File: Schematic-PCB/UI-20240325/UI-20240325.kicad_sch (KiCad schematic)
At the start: 0 parts

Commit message: UI基板の回路図を更新
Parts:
- added BZ1: Buzzer, symbol Device:Buzzer
- added J1: Conn_01x10_Pin, symbol Connector:Conn_01x10_Pin
- added R1, R3, R5, R6, R9: 1K, symbol Device:R_Small
- added R10, R2, R4, R7, R8: 10K, symbol Device:R_Small
- added SW1, SW2: SW_SPDT, symbol Switch:SW_SPDT
- added SW3, SW4, SW5: SW_Push, symbol Switch:SW_Push
- added U1: ~, symbol @2024-UI:Display
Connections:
- new net: R5.2, R7.2, SW3.1
- new net: R10.2, R9.2, SW5.1
- new net: R1.2, R2.2, SW1.2 (B)
- new net: R3.2, R4.2, SW2.2 (B)
- new net: R6.2, R8.2, SW4.1
- new net +3.3V: J1.1 (Pin_1), SW1.1 (A), SW2.1 (A), SW3.2, SW4.2, SW5.2, U1. (VCC)
- new net BUZZER: BZ1.1 (+), J1.10 (Pin_10)
- new net GND: BZ1.2 (-), J1.2 (Pin_2), R10.1, R2.1, R4.1, R7.1, R8.1, U1. (VCC)
- new net SCL: J1.9 (Pin_9), U1. (VCC)
- new net SDA: J1.8 (Pin_8), U1. (VCC)
- new net SW-TAC-1: J1.5 (Pin_5), R5.1
- new net SW-TAC-2: J1.6 (Pin_6), R6.1
- new net SW-TAC-3: J1.7 (Pin_7), R9.1
- new net SW-TOG-1: J1.4 (Pin_4), R1.1
- new net SW-TOG-2: J1.3 (Pin_3), R3.1
- no-connect marks 0 -> 2
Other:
- note added: "BUZZER"
- note added: "DISPLAY"
- note added: "TACTILE"
- note added: "TO MAIN"
- note added: "TOGGLE"

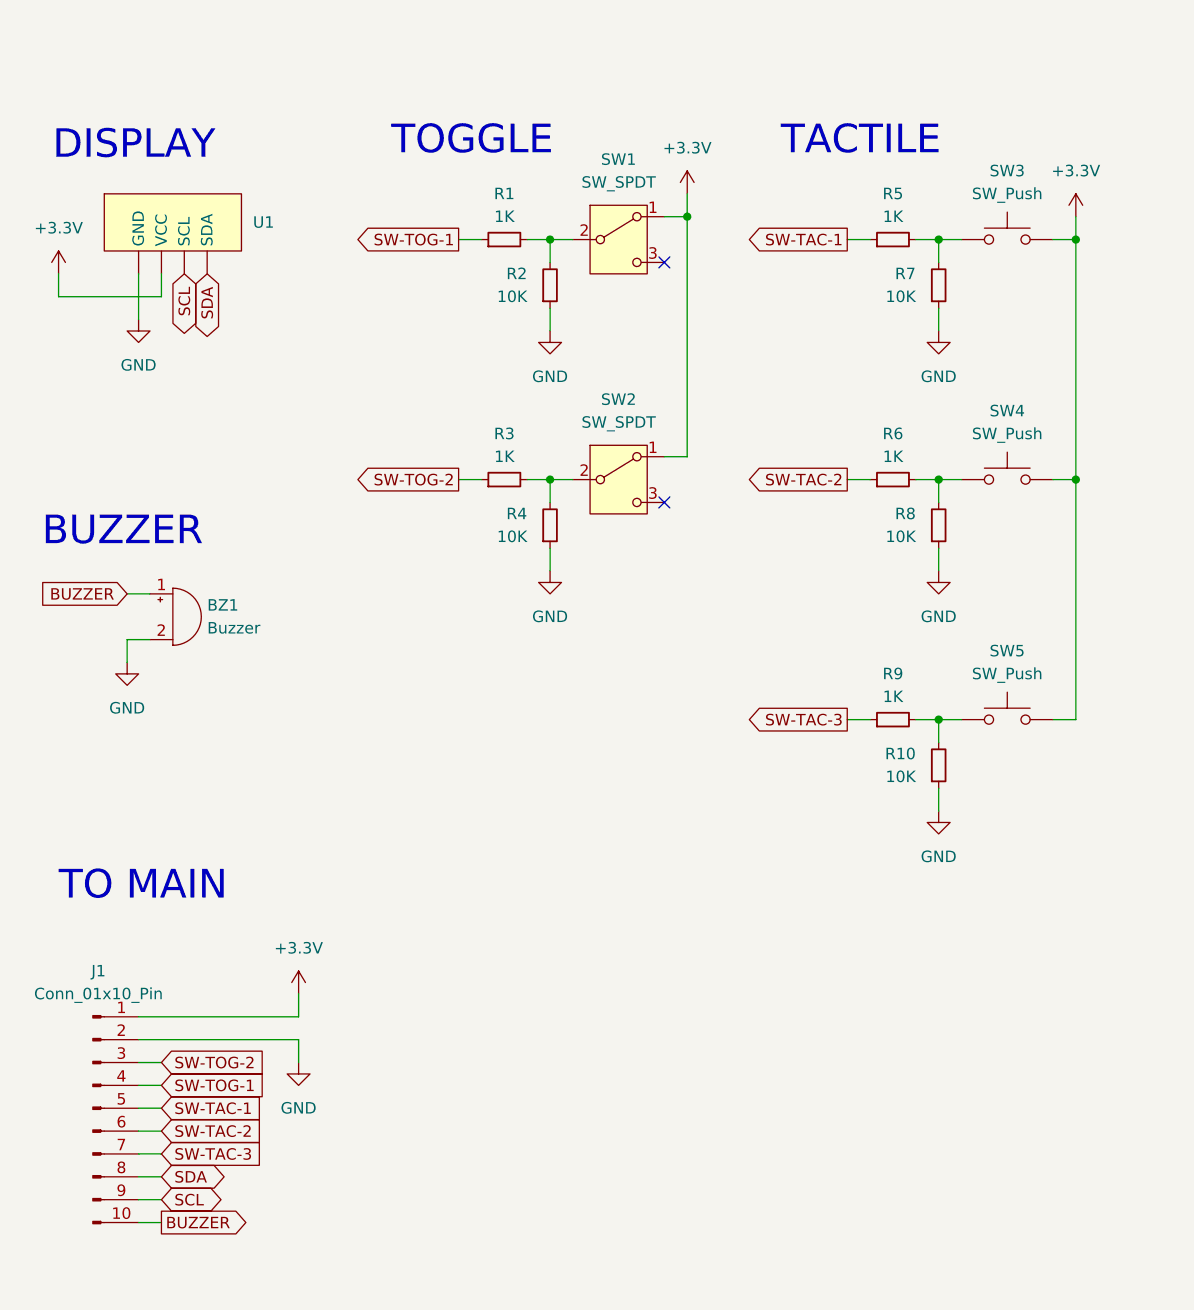
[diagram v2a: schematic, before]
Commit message: UI基板のPCBデザインを作成
決定ボタンのみフットプリントが決定しておらず未完成
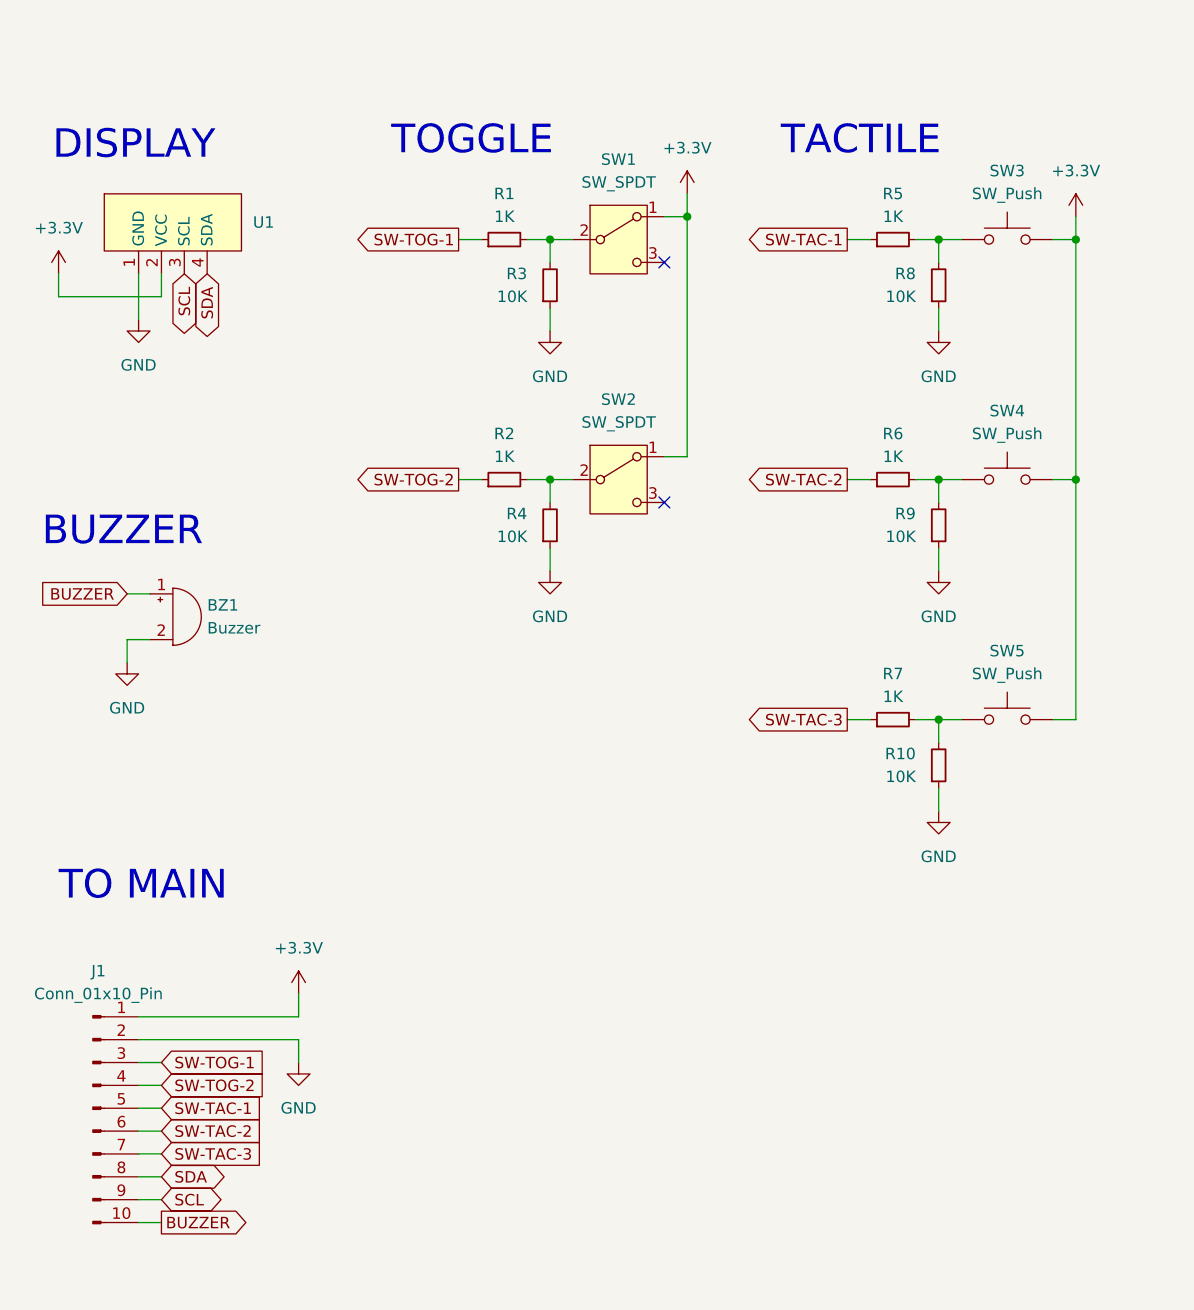
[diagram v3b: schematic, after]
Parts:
- BZ1: footprint (none) -> @2024-UI:PKM13EPYH4000-A0
- J1: footprint (none) -> Connector_JST:JST_XH_B10B-XH-A_1x10_P2.50mm_Vertical
- R1, R10, R4, R5, R6: footprint (none) -> Resistor_SMD:R_0603_1608Metric
- R2: renamed from R3; footprint (none) -> Resistor_SMD:R_0603_1608Metric
- R3: renamed from R2; footprint (none) -> Resistor_SMD:R_0603_1608Metric
- R7: renamed from R9; footprint (none) -> Resistor_SMD:R_0603_1608Metric
- R8: renamed from R7; footprint (none) -> Resistor_SMD:R_0603_1608Metric
- R9: renamed from R8; footprint (none) -> Resistor_SMD:R_0603_1608Metric
- SW1, SW2: footprint (none) -> @2024-UI:2MS1-T1-B4-VS2-Q-E-S
- SW3, SW5: footprint (none) -> @2024-UI:TVBP06-B043C
- U1: footprint (none) -> @2024-UI:Display
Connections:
- net +3.3V: now also U1.2 (VCC); no longer U1. (VCC)
- net GND: now also U1.1 (GND); no longer U1. (VCC)
- net SCL: now also U1.3 (SCL); no longer U1. (VCC)
- net SDA: now also U1.4 (SDA); no longer U1. (VCC)
- net SW-TOG-1: now also J1.3 (Pin_3); no longer J1.4 (Pin_4)
- net SW-TOG-2: now also J1.4 (Pin_4); no longer J1.3 (Pin_3)

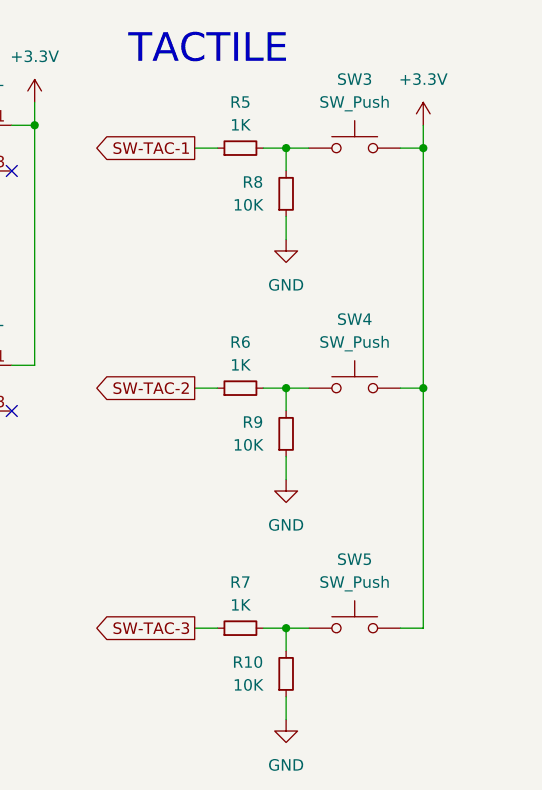
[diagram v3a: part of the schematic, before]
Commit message: Ui基板の回路図・PCBデザインを更新しました
DR & 修正・SW-4に関する変更
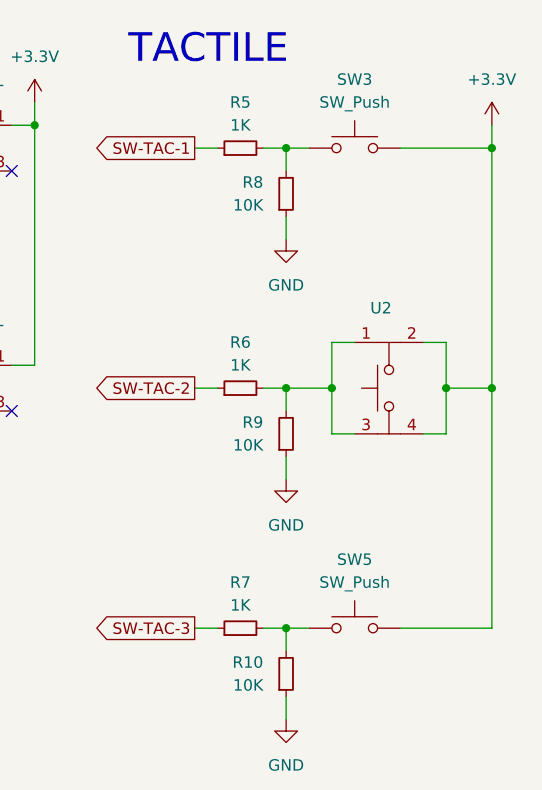
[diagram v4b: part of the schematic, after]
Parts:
- removed SW4: SW_Push, symbol Switch:SW_Push
- added U2: ~, @2024-UI:TVGP01-G73BB, symbol @2024-UI:TVGP01-G73BB
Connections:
- net +3.3V: now also U2.2, U2.4
- net at R6.2, R9.2: now also U2.1, U2.3
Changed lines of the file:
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@@
 	(paper "A4")
 	(junction
-		(at 140.97 50.8)
+		(at 148.59 50.8)
+		(diameter 0)
+		(color 0 0 0 0)
+	)
+	(junction
+		(at 148.59 77.47)
 		(diameter 0)
 		(color 0 0 0 0)
@@
 	)
 	(junction
-		(at 140.97 77.47)
+		(at 143.51 77.47)
 		(diameter 0)
 		(color 0 0 0 0)
@@
 		(color 0 0 0 0)
 	)
+	(junction
+		(at 130.81 77.47)
+		(diameter 0)
+		(color 0 0 0 0)
+	)
 	(no_connect
 		(at 95.25 80.01)
@@
 	(wire
 		(pts
+			(xy 133.35 82.55) (xy 130.81 82.55)
+		)
+		(stroke
+			(width 0)
+			(type default)
+		)
+	)
+	(wire
+		(pts
 			(xy 82.55 53.34) (xy 82.55 50.8)
 		)
@@
 	(wire
 		(pts
-			(xy 140.97 50.8) (xy 140.97 77.47)
+			(xy 148.59 50.8) (xy 148.59 77.47)
 		)
 		(stroke
@@
 	(wire
 		(pts
-			(xy 138.43 50.8) (xy 140.97 50.8)
-		)
-		(stroke
-			(width 0)
-			(type default)
-		)
-	)
-	(wire
-		(pts
-			(xy 138.43 77.47) (xy 140.97 77.47)
-		)
-		(stroke
-			(width 0)
-			(type default)
-		)
-	)
-	(wire
-		(pts
 			(xy 36.83 154.94) (xy 39.37 154.94)
 		)
@@
 	(wire
 		(pts
-			(xy 138.43 104.14) (xy 140.97 104.14)
-		)
-		(stroke
-			(width 0)
-			(type default)
-		)
-	)
-	(wire
-		(pts
 			(xy 72.39 50.8) (xy 74.93 50.8)
 		)
@@
 	(wire
 		(pts
+			(xy 140.97 72.39) (xy 143.51 72.39)
+		)
+		(stroke
+			(width 0)
+			(type default)
+		)
+	)
+	(wire
+		(pts
 			(xy 36.83 54.61) (xy 36.83 59.69)
 		)
@@
 	(wire
 		(pts
+			(xy 143.51 77.47) (xy 148.59 77.47)
+		)
+		(stroke
+			(width 0)
+			(type default)
+		)
+	)
+	(wire
+		(pts
 			(xy 123.19 104.14) (xy 125.73 104.14)
 		)
@@
 	(wire
 		(pts
+			(xy 138.43 104.14) (xy 148.59 104.14)
+		)
+		(stroke
+			(width 0)
+			(type default)
+		)
+	)
+	(wire
+		(pts
 			(xy 115.57 104.14) (xy 118.11 104.14)
 		)
@@
 	(wire
 		(pts
-			(xy 140.97 77.47) (xy 140.97 104.14)
+			(xy 130.81 82.55) (xy 130.81 77.47)
 		)
 		(stroke
@@
 	(wire
 		(pts
-			(xy 140.97 48.26) (xy 140.97 50.8)
+			(xy 148.59 48.26) (xy 148.59 50.8)
 		)
 		(stroke
@@
 	(wire
 		(pts
+			(xy 148.59 77.47) (xy 148.59 104.14)
+		)
+		(stroke
+			(width 0)
+			(type default)
+		)
+	)
+	(wire
+		(pts
+			(xy 143.51 82.55) (xy 140.97 82.55)
+		)
+		(stroke
+			(width 0)
+			(type default)
+		)
+	)
+	(wire
+		(pts
 			(xy 54.61 139.7) (xy 54.61 142.24)
 		)
@@
 	(wire
 		(pts
+			(xy 130.81 72.39) (xy 130.81 77.47)
+		)
+		(stroke
+			(width 0)
+			(type default)
+		)
+	)
+	(wire
+		(pts
 			(xy 39.37 57.15) (xy 27.94 57.15)
 		)
@@
 	(wire
 		(pts
-			(xy 125.73 77.47) (xy 128.27 77.47)
+			(xy 125.73 77.47) (xy 130.81 77.47)
 		)
 		(stroke
@@
 	(wire
 		(pts
+			(xy 143.51 77.47) (xy 143.51 82.55)
+		)
+		(stroke
+			(width 0)
+			(type default)
+		)
+	)
+	(wire
+		(pts
 			(xy 35.56 90.17) (xy 38.1 90.17)
 		)
@@
 	(wire
 		(pts
+			(xy 130.81 72.39) (xy 133.35 72.39)
+		)
+		(stroke
+			(width 0)
+			(type default)
+		)
+	)
+	(wire
+		(pts
 			(xy 36.83 142.24) (xy 39.37 142.24)
+		)
+		(stroke
+			(width 0)
+			(type default)
+		)
+	)
+	(wire
+		(pts
+			(xy 138.43 50.8) (xy 148.59 50.8)
+		)
+		(stroke
+			(width 0)
+			(type default)
+		)
+	)
+	(wire
+		(pts
+			(xy 143.51 72.39) (xy 143.51 77.47)
 		)
 		(stroke
@@
 	(symbol
 		(lib_id "power:+3.3V")
-		(at 140.97 48.26 0)
+		(at 148.59 48.26 0)
 		(unit 1)
 		(exclude_from_sim no)
@@
 		(fields_autoplaced yes)
 		(property "Reference" "#PWR012"
-			(at 140.97 52.07 0)
+			(at 148.59 52.07 0)
 			(effects
 				(font
@@
 		)
 		(property "Value" "+3.3V"
-			(at 140.97 43.18 0)
+			(at 148.59 43.18 0)
 			(effects
 				(font
@@
 		)
 		(property "Footprint" ""
-			(at 140.97 48.26 0)
+			(at 148.59 48.26 0)
 			(effects
 				(font
@@
 		)
 		(property "Datasheet" ""
-			(at 140.97 48.26 0)
+			(at 148.59 48.26 0)
 			(effects
 				(font
@@
 		)
 		(property "Description" "Power symbol creates a global label with name \"+3.3V\""
-			(at 140.97 48.26 0)
+			(at 148.59 48.26 0)
 			(effects
 				(font
@@
 	)
 	(symbol
+		(lib_id "@2024-UI:TVGP01-G73BB")
+		(at 137.16 77.47 0)
+		(unit 1)
+		(exclude_from_sim no)
+		(in_bom yes)
+		(on_board yes)
+		(dnp no)
+		(fields_autoplaced yes)
+		(property "Reference" "U2"
+			(at 136.271 68.58 0)
+			(effects
+				(font
+					(size 1.27 1.27)
+				)
+			)
+		)
+		(property "Value" "~"
+			(at 136.271 71.12 0)
+			(effects
+				(font
+					(size 1.27 1.27)
+				)
+			)
+		)
+		(property "Footprint" "@2024-UI:TVGP01-G73BB"
+			(at 138.43 77.47 90)
+			(effects
+				(font
+					(size 1.27 1.27)
+				)
+				(hide yes)
+			)
+		)
+		(property "Datasheet" ""
+			(at 138.43 77.47 90)
+			(effects
+				(font
+					(size 1.27 1.27)
+				)
+				(hide yes)
+			)
+		)
+		(property "Description" ""
+			(at 138.43 77.47 90)
+			(effects
+				(font
+					(size 1.27 1.27)
+				)
+				(hide yes)
+			)
+		)
+		(pin "1"
+		)
+		(pin "4"
+		)
+		(pin "3"
+		)
+		(pin "2"
+		)
+		(instances
+			(project "UI-20240325"
+				(path "/cf415513-ce1b-482f-888f-072969d0dcb5"
+					(reference "U2")
+					(unit 1)
+				)
+			)
+		)
+	)
+	(symbol
 		(lib_id "power:GND")
 		(at 82.55 87.63 0)
@@
 					(unit 1)
 				)
-			)
-		)
-	)
-	(symbol
-		(lib_id "Switch:SW_Push")
-		(at 133.35 77.47 0)
-		(unit 1)
-		(exclude_from_sim no)
-		(in_bom yes)
-		(on_board yes)
-		(dnp no)
-		(fields_autoplaced yes)
-		(property "Reference" "SW4"
-			(at 133.35 69.85 0)
-			(effects
-				(font
-					(size 1.27 1.27)
-				)
-			)
-		)
-		(property "Value" "SW_Push"
-			(at 133.35 72.39 0)
-			(effects
-				(font
-					(size 1.27 1.27)
-				)
-			)
-		)
-		(property "Footprint" ""
-			(at 133.35 72.39 0)
-			(effects
-				(font
-					(size 1.27 1.27)
-				)
-				(hide yes)
-			)
-		)
-		(property "Datasheet" "~"
-			(at 133.35 72.39 0)
-			(effects
-				(font
-					(size 1.27 1.27)
-				)
-				(hide yes)
-			)
-		)
-		(property "Description" "Push button switch, generic, two pins"
-			(at 133.35 77.47 0)
-			(effects
-				(font
-					(size 1.27 1.27)
-				)
-				(hide yes)
-			)
-		)
-		(pin "2"
-		)
-		(pin "1"
-		)
-		(instances
-			(project "UI-20240325"
-				(path "/cf415513-ce1b-482f-888f-072969d0dcb5"
-					(reference "SW4")
-					(unit 1)
-				)
